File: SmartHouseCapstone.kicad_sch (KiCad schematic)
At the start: 0 parts

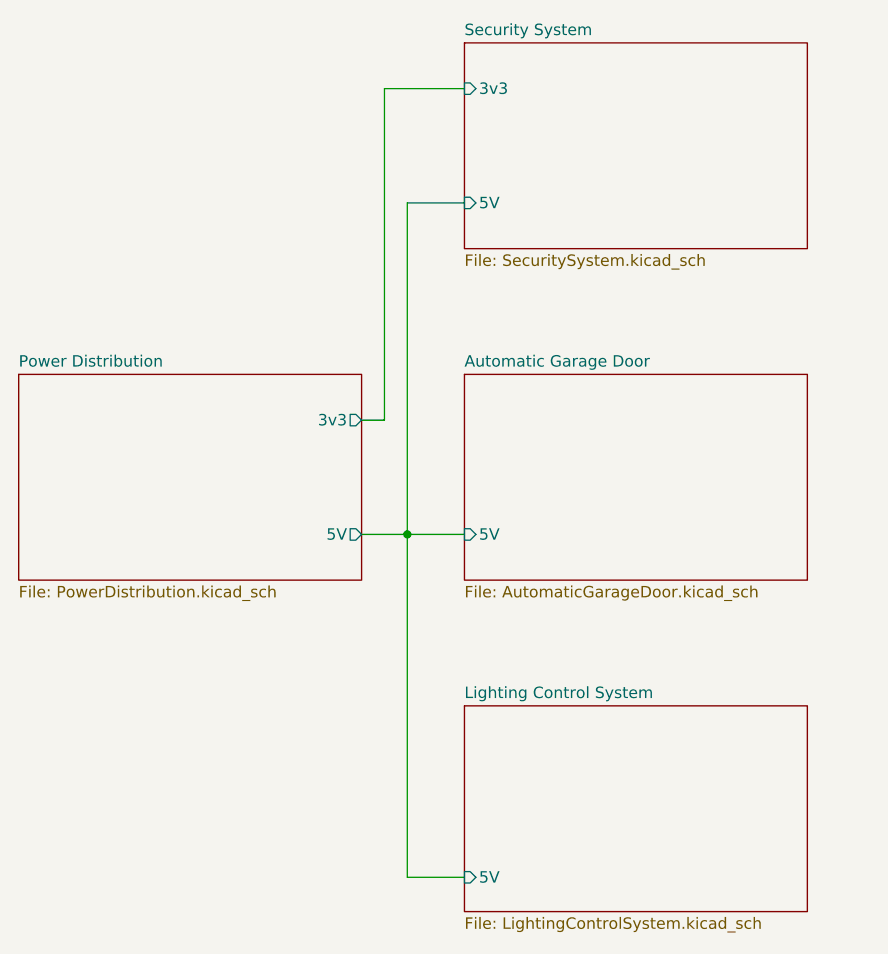
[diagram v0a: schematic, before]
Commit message: revision 2
modified pull-up/pull-down resistor values
modified switch1/switch2 input voltage from 5V to 3v3

added proper sheet detail (designer, cc license)
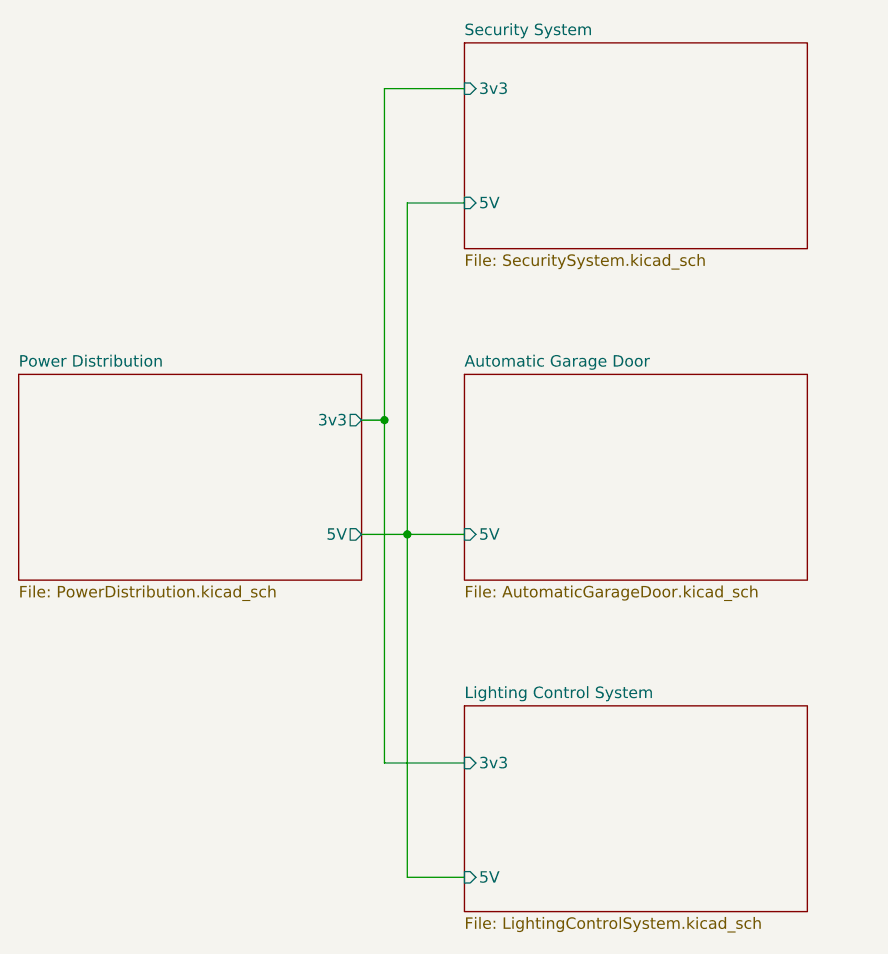
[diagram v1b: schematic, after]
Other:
- sheet Lighting Control System ports: added 3v3; removed none
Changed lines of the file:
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@@
 		(title "Smart Home Capstone")
 		(date "2025-10-31")
-		(rev "0")
+		(rev "2")
+		(comment 1 "Designed by: Sidney Manzano")
+		(comment 2 "Released under the Creative Commons")
+		(comment 3 "Attribution Share-Alike 4.0 License")
+		(comment 4 "https://creativecommons.org/licenses/by-sa/4.0")
+	)
+	(junction
+		(at 102.87 73.66)
+		(diameter 0)
+		(color 0 0 0 0)
 	)
 	(junction
@@
 	(wire
 		(pts
-			(xy 102.87 73.66) (xy 100.33 73.66)
+			(xy 102.87 111.76) (xy 111.76 111.76)
+		)
+		(stroke
+			(width 0)
+			(type default)
+		)
+	)
+	(wire
+		(pts
+			(xy 100.33 73.66) (xy 102.87 73.66)
 		)
 		(stroke
@@
 		(pts
 			(xy 102.87 36.83) (xy 102.87 73.66)
+		)
+		(stroke
+			(width 0)
+			(type default)
+		)
+	)
+	(wire
+		(pts
+			(xy 102.87 73.66) (xy 102.87 111.76)
 		)
 		(stroke
@@
 			(effects
 				(font
+					(size 1.27 1.27)
+				)
+				(justify left)
+			)
+		)
+		(pin "3v3" input
+			(at 111.76 111.76 180)
+			(effects
+				(font
